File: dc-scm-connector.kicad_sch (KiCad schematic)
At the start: 10 parts, among them J19 Socket_Amphenol_ME10168134011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

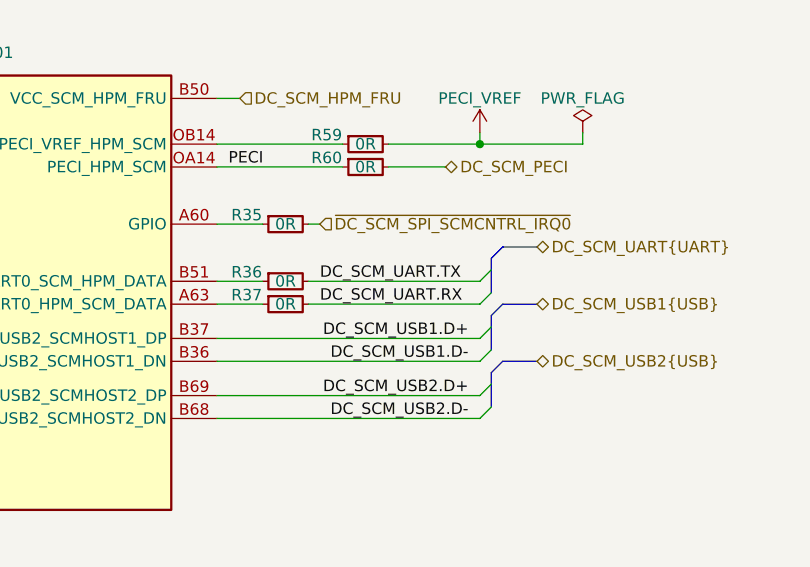
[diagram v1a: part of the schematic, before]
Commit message: [#92504] Add QWIIC sheet
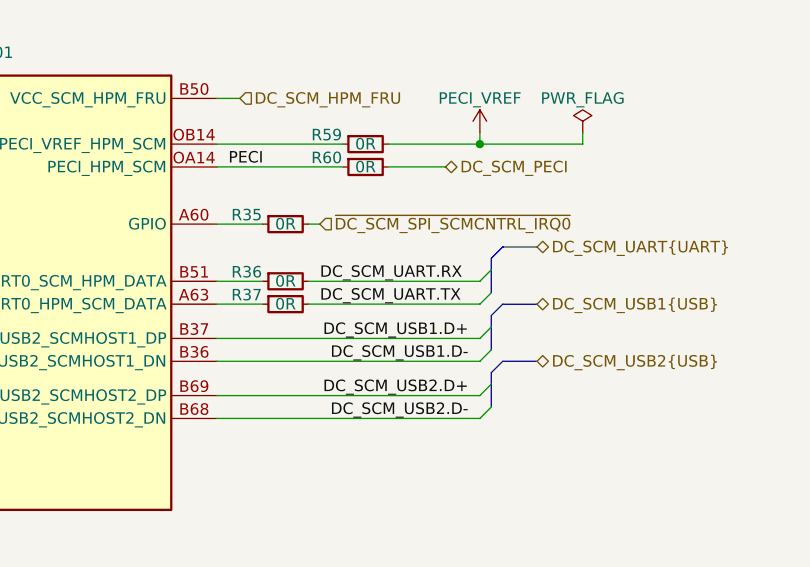
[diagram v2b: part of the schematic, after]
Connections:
- net DC_SCM_UART.RX: now also R36.2; no longer R37.2
- net DC_SCM_UART.TX: now also R37.2; no longer R36.2
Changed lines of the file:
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@@
 	)
 	(label "DC_SCM_UART.TX"
-		(at 158.75 64.77 0)
+		(at 158.75 67.31 0)
 		(effects
 			(font
@@
 	)
 	(label "DC_SCM_UART.RX"
-		(at 158.75 67.31 0)
+		(at 158.75 64.77 0)
 		(effects
 			(font

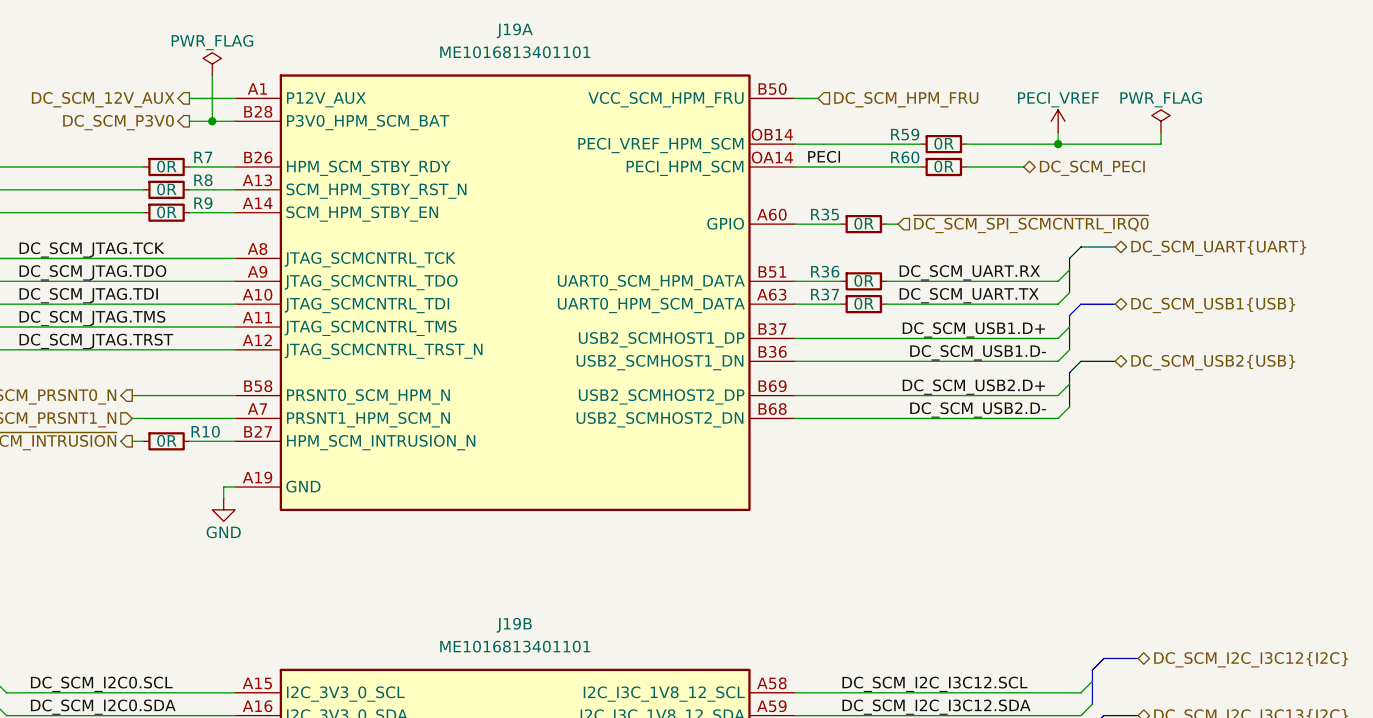
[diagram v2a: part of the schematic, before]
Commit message: [#92504] Add HOST USB type A
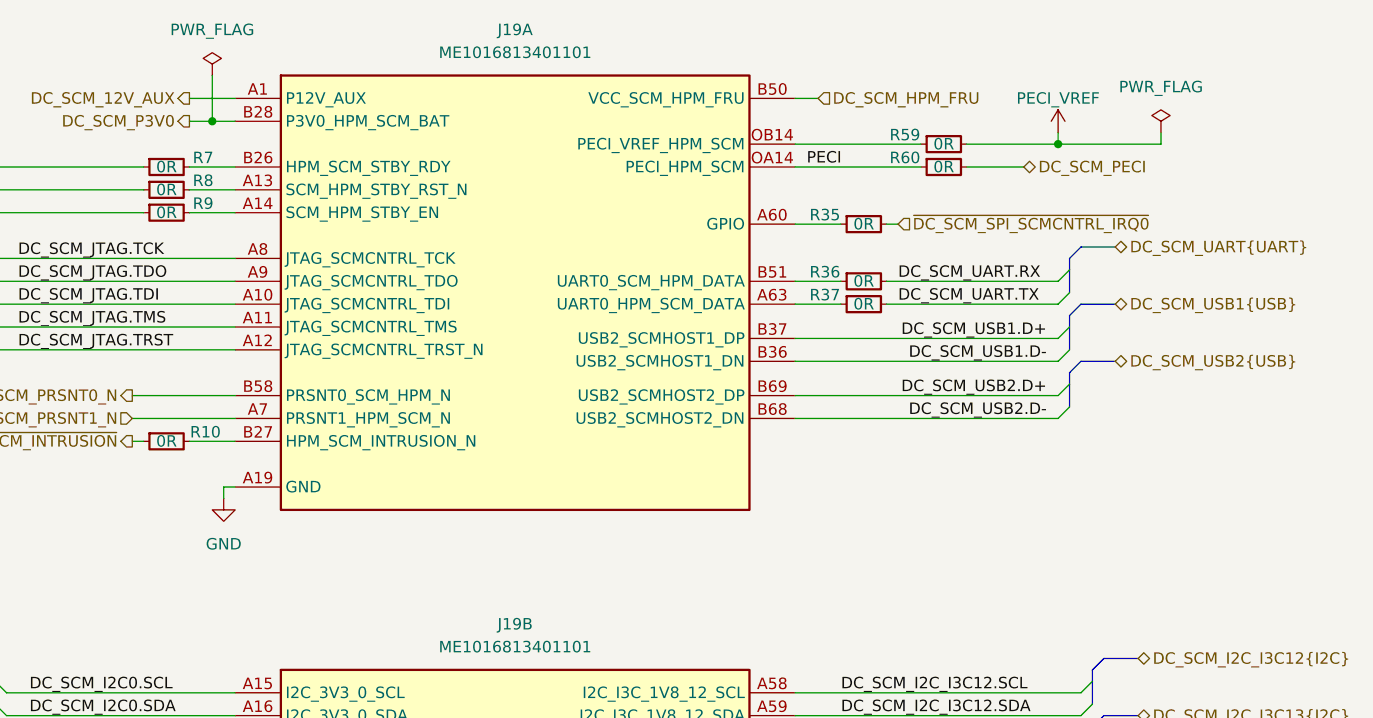
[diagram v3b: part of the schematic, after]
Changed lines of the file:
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@@
 		(rev "1.1.0")
 	)
+	(bus_alias "DP"
+		(members "TXD0-" "TXD0+" "TXD1-" "TXD1+" "TXD2-" "TXD2+" "TXD3-" "TXD3+"
+			"HPD" "AUX-" "AUX+"
+		)
+	)
+	(bus_alias "DSI"
+		(members "D0+" "D0-" "D1+" "D1-" "D2+" "D2-" "D3+" "D3-" "CLK+" "CLK-")
+	)
+	(bus_alias "ETHERNET"
+		(members "MDI0-" "MDI0+" "MDI1-" "MDI1+" "MDI2-" "MDI2+" "MDI3-" "MDI3+")
+	)
 	(bus_alias "I2C"
 		(members "SCL" "SDA")
 	)
+	(bus_alias "I3C"
+		(members "SCL" "SDA")
+	)
+	(bus_alias "JTAG"
+		(members "TCK" "TDO" "TDI" "TMS" "TRST")
+	)
+	(bus_alias "LTPI"
+		(members "RXD-" "RXD+" "TXD-" "TXD+" "RXCK+" "RXCK-" "TXCK+" "TXCK-")
+	)
+	(bus_alias "NC-SI"
+		(members "REF_CLK" "CRS_DV" "RXD[0..1]" "TX_EN" "TXD[0..1]")
+	)
+	(bus_alias "PCIE"
+		(members "RX0+" "RX0-" "TX0+" "TX0-" "RX1+" "RX1-" "TX1+" "TX1-" "RX2+"
+			"RX2-" "TX2+" "TX2-" "RX3+" "RX3-" "TX3+" "TX3-"
+		)
+	)
+	(bus_alias "PCIeREFCLK"
+		(members "CLK+" "CLK-")
+	)
+	(bus_alias "QSPI"
+		(members "IO0" "IO1" "IO2" "IO3" "SCK" "~{CS0}" "~{CS1}")
+	)
+	(bus_alias "RGMII"
+		(members "TXD0" "TXD1" "TXD2" "TXD3" "RXD0" "RXD1" "RXD2" "RXD3" "TX_CLK"
+			"TX_CTL" "RX_CTL" "RX_CLK" "MDIO" "MDC"
+		)
+	)
+	(bus_alias "SDIO"
+		(members "DAT[0..7]" "CMD" "CLK" "~{CD}" "IOPWR" "PWR_EN" "WP" "DS")
+	)
+	(bus_alias "SGMII"
+		(members "TX+" "TX-" "RX+" "RX-")
+	)
+	(bus_alias "SPI"
+		(members "DO" "DI" "SCK" "~{CS0}" "~{CS1}")
+	)
+	(bus_alias "STBY_1V8"
+		(members "RDY" "EN" "~{RST_N}")
+	)
+	(bus_alias "STBY_3V3"
+		(members "RDY" "EN" "~{RST_N}")
+	)
+	(bus_alias "UART"
+		(members "RX" "TX")
+	)
+	(bus_alias "USB"
+		(members "D+" "D-")
+	)
+	(bus_alias "USBSS"
+		(members "RX+" "RX-" "TX+" "TX-")
+	)
+	(bus_alias "eSPI"
+		(members "IO0" "IO1" "IO2" "IO3" "SCK" "~{CS0}" "~{ALERT0}" "~{RESET}")
+	)
 	(text "PCIe directions from HPM POV\n"
 		(exclude_from_sim no)
@@
 	)
 	(symbol
+		(lib_name "PWR_FLAG_1")
+		(lib_id "antmicropower:PWR_FLAG")
+		(at 82.55 41.91 0)
+		(unit 1)
+		(exclude_from_sim no)
+		(in_bom yes)
+		(on_board yes)
+		(dnp no)
+		(fields_autoplaced yes)
+		(property "Reference" "#FLG05"
+			(at 82.55 40.005 0)
+			(effects
+				(font
+					(size 1.27 1.27)
+				)
+				(hide yes)
+			)
+		)
+		(property "Value" "PWR_FLAG"
+			(at 82.55 36.83 0)
+			(effects
+				(font
+					(size 1.27 1.27)
+				)
+			)
+		)
+		(property "Footprint" ""
+			(at 82.55 41.91 0)
+			(effects
+				(font
+					(size 1.27 1.27)
+				)
+				(hide yes)
+			)
+		)
+		(property "Datasheet" ""
+			(at 82.55 41.91 0)
+			(effects
+				(font
+					(size 1.27 1.27)
+				)
+				(hide yes)
+			)
+		)
+		(property "Description" ""
+			(at 82.55 44.45 0)
+			(effects
+				(font
+					(size 1.27 1.27)
+				)
+				(justify left bottom)
+				(hide yes)
+			)
+		)
+		(pin "1"
+		)
+		(instances
+			(project ""
+				(path "/5d67ef28-5805-4f87-b722-2926dabf7f6e/bae8cef5-57a9-4ec0-acbe-6dac48c5cdf5"
+					(reference "#FLG05")
+					(unit 1)
+				)
+			)
+		)
+	)
+	(symbol
 		(lib_id "antmicroResistors0402:R_0R_0402")
 		(at 74.93 57.15 0)
@@
 	)
 	(symbol
+		(lib_name "PWR_FLAG_1")
 		(lib_id "antmicropower:PWR_FLAG")
-		(at 82.55 41.91 0)
+		(at 187.96 48.26 0)
 		(unit 1)
 		(exclude_from_sim no)
@@
 		(on_board yes)
 		(dnp no)
+		(fields_autoplaced yes)
 		(property "Reference" "#FLG01"
-			(at 82.55 40.005 0)
+			(at 187.96 46.355 0)
 			(effects
 				(font
@@
 		)
 		(property "Value" "PWR_FLAG"
-			(at 82.55 38.1 0)
+			(at 187.96 43.18 0)
 			(effects
 				(font
@@
 		)
 		(property "Footprint" ""
-			(at 82.55 41.91 0)
+			(at 187.96 48.26 0)
 			(effects
 				(font
@@
 		)
 		(property "Datasheet" ""
-			(at 82.55 41.91 0)
+			(at 187.96 48.26 0)
 			(effects
 				(font
@@
 		)
 		(property "Description" ""
-			(at 82.55 41.91 0)
+			(at 187.96 50.8 0)
 			(effects
 				(font
 					(size 1.27 1.27)
 				)
+				(justify left bottom)
 				(hide yes)
 			)
@@
 	)
 	(symbol
+		(lib_name "GND_1")
 		(lib_id "antmicropower:GND")
 		(at 83.82 88.9 0)
@@
 		(on_board yes)
 		(dnp no)
-		(property "Reference" "#PWR02"
+		(fields_autoplaced yes)
+		(property "Reference" "#PWR038"
 			(at 92.71 91.44 0)
 			(effects
@@
 		)
 		(property "Value" "GND"
-			(at 83.82 92.71 0)
+			(at 83.82 93.98 0)
 			(effects
 				(font
@@
 		)
 		(property "Description" ""
-			(at 83.82 88.9 0)
+			(at 92.71 104.14 0)
 			(effects
 				(font
 					(size 1.27 1.27)
 				)
+				(justify left bottom)
 				(hide yes)
 			)
@@
 		)
 		(instances
-			(project "bmc-breakout-board"
-				(path "/5d67ef28-5805-4f87-b722-2926dabf7f6e/bae8cef5-57a9-4ec0-acbe-6dac48c5cdf5"
-					(reference "#PWR02")
-					(unit 1)
-				)
-			)
-		)
-	)
-	(symbol
-		(lib_id "antmicropower:PWR_FLAG")
-		(at 187.96 48.26 0)
-		(unit 1)
-		(exclude_from_sim no)
-		(in_bom yes)
-		(on_board yes)
-		(dnp no)
-		(property "Reference" "#FLG02"
-			(at 187.96 46.355 0)
-			(effects
-				(font
-					(size 1.27 1.27)
-				)
-				(hide yes)
-			)
-		)
-		(property "Value" "PWR_FLAG"
-			(at 187.96 44.45 0)
-			(effects
-				(font
-					(size 1.27 1.27)
-				)
-			)
-		)
-		(property "Footprint" ""
-			(at 187.96 48.26 0)
-			(effects
-				(font
-					(size 1.27 1.27)
-				)
-				(hide yes)
-			)
-		)
-		(property "Datasheet" ""
-			(at 187.96 48.26 0)
-			(effects
-				(font
-					(size 1.27 1.27)
-				)
-				(hide yes)
-			)
-		)
-		(property "Description" ""
-			(at 187.96 48.26 0)
-			(effects
-				(font
-					(size 1.27 1.27)
-				)
-				(hide yes)
-			)
-		)
-		(pin "1"
-		)
-		(instances
-			(project "bmc-breakout-board"
+			(project ""
 				(path "/5d67ef28-5805-4f87-b722-2926dabf7f6e/bae8cef5-57a9-4ec0-acbe-6dac48c5cdf5"
-					(reference "#FLG02")
+					(reference "#PWR038")
 					(unit 1)
 				)

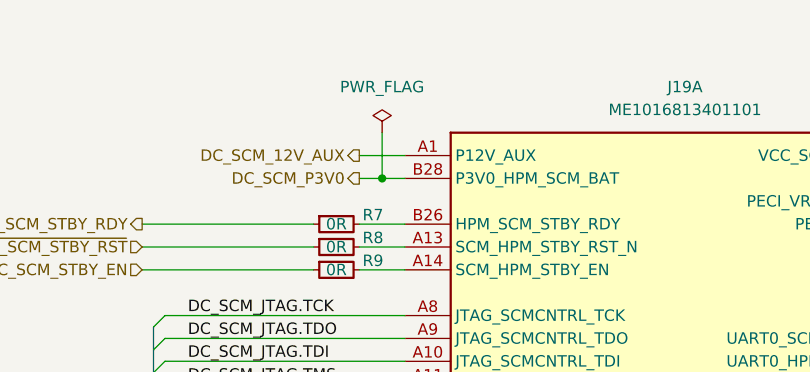
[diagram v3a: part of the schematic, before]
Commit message: [#92504] Clear Wire BUS errors
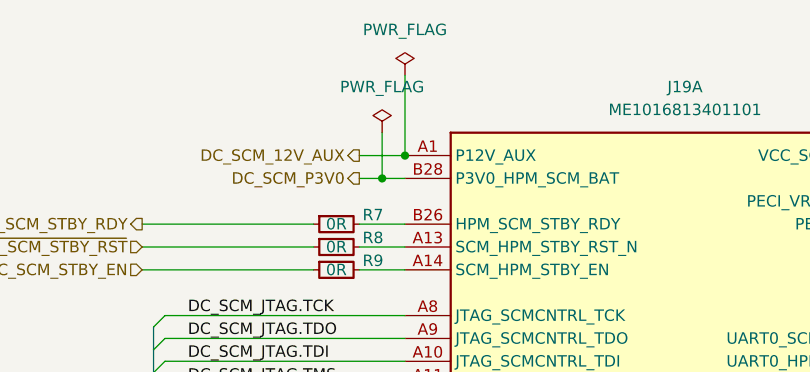
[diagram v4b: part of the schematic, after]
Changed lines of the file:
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@@
 	)
 	(junction
+		(at 85.09 44.45)
+		(diameter 0)
+		(color 0 0 0 0)
+	)
+	(junction
 		(at 82.55 46.99)
 		(diameter 0)
@@
 		)
 	)
+	(wire
+		(pts
+			(xy 85.09 35.56) (xy 85.09 44.45)
+		)
+		(stroke
+			(width 0)
+			(type default)
+		)
+	)
 	(bus
 		(pts
@@
 					(unit 1)
 				)
+			)
+		)
+	)
+	(symbol
+		(lib_name "PWR_FLAG_1")
+		(lib_id "antmicropower:PWR_FLAG")
+		(at 85.09 35.56 0)
+		(unit 1)
+		(exclude_from_sim no)
+		(in_bom yes)
+		(on_board yes)
+		(dnp no)
+		(fields_autoplaced yes)
+		(property "Reference" "#FLG02"
+			(at 85.09 33.655 0)
+			(effects
+				(font
+					(size 1.27 1.27)
+				)
+				(hide yes)
+			)
+		)
+		(property "Value" "PWR_FLAG"
+			(at 85.09 30.48 0)
+			(effects
+				(font
+					(size 1.27 1.27)
+				)
+			)
+		)
+		(property "Footprint" ""
+			(at 85.09 35.56 0)
+			(effects
+				(font
+					(size 1.27 1.27)
+				)
+				(hide yes)
+			)
+		)
+		(property "Datasheet" ""
+			(at 85.09 35.56 0)
+			(effects
+				(font
+					(size 1.27 1.27)
+				)
+				(hide yes)
+			)
+		)
+		(property "Description" ""
+			(at 85.09 38.1 0)
+			(effects
+				(font
+					(size 1.27 1.27)
+				)
+				(justify left bottom)
+				(hide yes)
+			)
+		)
+		(pin "1"
+		)
+		(instances
+			(project "bmc-breakout-board"
+				(path "/5d67ef28-5805-4f87-b722-2926dabf7f6e/bae8cef5-57a9-4ec0-acbe-6dac48c5cdf5"
+					(reference "#FLG02")
+					(unit 1)
+				)

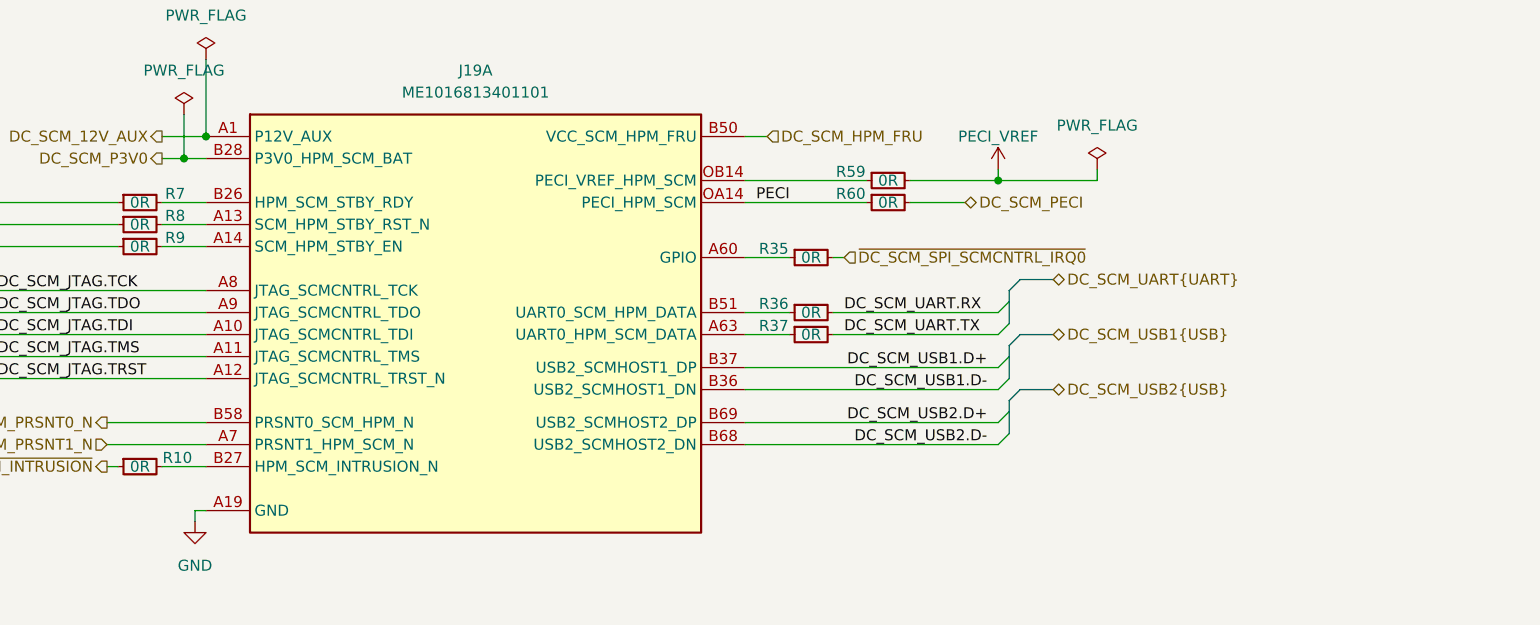
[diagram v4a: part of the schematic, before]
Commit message: [#92504] Clear ERC errors
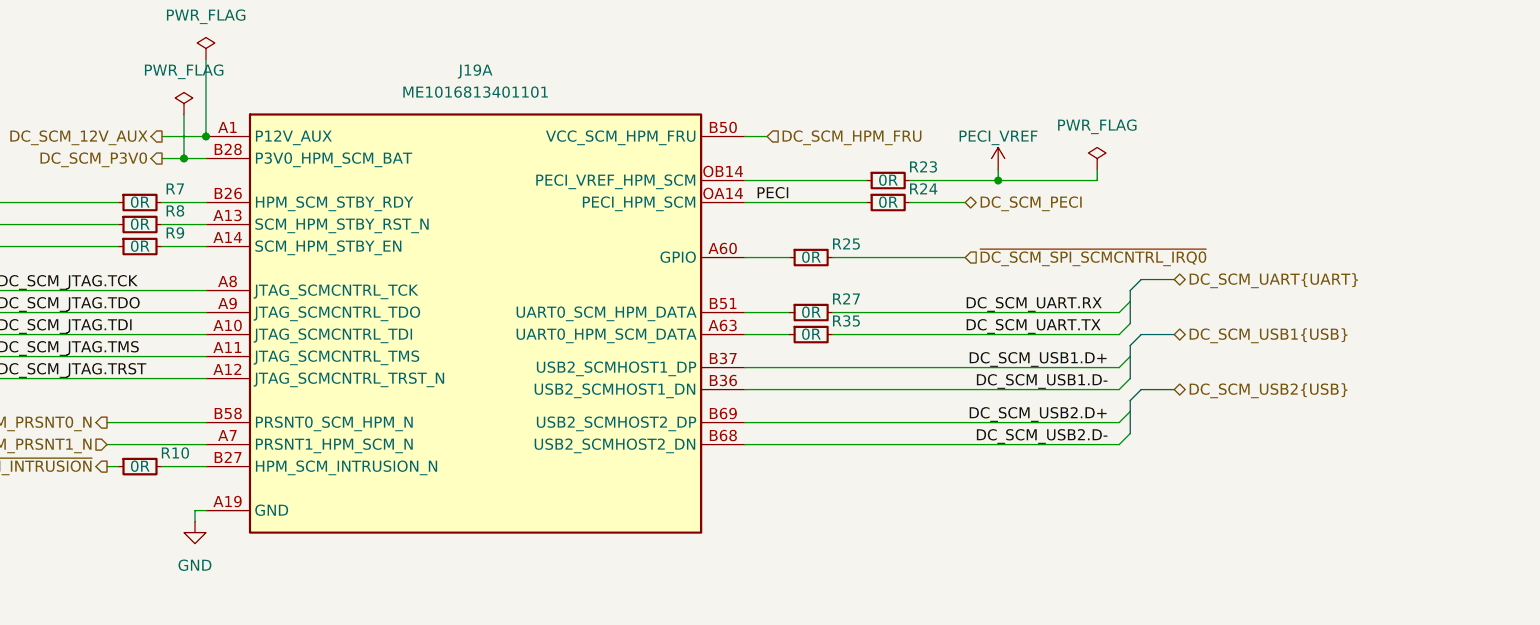
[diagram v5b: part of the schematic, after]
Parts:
- removed R36, R37, R59, R60: R_0R_0402, antmicro-footprints:R_0402_1005Metric, symbol antmicroResistors0402:R_0R_0402
- added R23, R24, R25, R27: R_0R_0402, antmicro-footprints:R_0402_1005Metric, symbol antmicroResistors0402:R_0R_0402
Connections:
- net DC_SCM_PECI: now also R24.2
- net DC_SCM_UART.RX: now also R27.2
- net DC_SCM_UART.TX: now also R35.2
- net PECI: now also R24.1
- net PECI_VREF: now also R23.2
- net ~{DC_SCM_SPI_SCMCNTRL_IRQ0}: now also R25.2; no longer R35.2
- net at J19.A60 (GPIO): now also R25.1; no longer R35.1
- net at J19.OB14 (PECI_VREF_HPM_SCM): now also R23.1
- net at J19.A63 (UART0_HPM_SCM_DATA): now also R35.1
- net at J19.B51 (UART0_SCM_HPM_DATA): now also R27.1
